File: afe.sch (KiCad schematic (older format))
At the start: 48 parts, among them J2 Conn_01x05, Q5 2N7002, Q6 2N7002, U10 TS5A2053, U11 ADS7946SRTET, U5 REF2915, U6 TCA9535MRGER, U7 TLV9062S, U8 OPA2322S, U9 TS5A2053

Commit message: *white smoke*
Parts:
- added C?: 100n, Capacitor_SMD:C_0603_1608Metric, symbol Device:C_Small
- added FB?: Ferret, symbol Device:Ferrite_Bead_Small
- added Q?: 2N7002, Package_TO_SOT_SMD:SOT-23, symbol Transistor_FET:2N7002
- added R?: 47k, Resistor_SMD:R_0603_1608Metric, symbol Device:R
- added U?: USBLC6-2SC6, Package_TO_SOT_SMD:SOT-23-6, symbol Power_Protection:USBLC6-2SC6
- R10, R9: value 100k -> 47k
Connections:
- net +3V3: now also U11.16 (DVDD), FB?.2, R?.2, U?.5 (VBUS)
- net AFE_ENABLE: now also Q?.1 (G)
- net GND: now also U11.17 (EPAD), Q?.2 (S), U?.2 (GND)
- net GNDA: now also C?.2; no longer C24.2, C25.2
- net PROBE1: now also U?.4 (IO2)
- net PROBE2: now also U?.3 (IO2)
- net ADC_CH_SEL: now reaches U11.11 (CH_SEL)
- net ADC_ENABLE: now reaches U11.12 (PDEN)
- net ADC_ENABLE: now also Q?.3 (D), R?.1
- net ADC_CS: now reaches U11.13 (~CS~)
- net ADC_SCK: now reaches U11.14 (SCLK)
- net ADC_MISO: now reaches U11.15 (SDO)
- net at U11.2 (AVDD): now also C?.1, FB?.1
- net at J2.3 (Pin_3), R11.1, R12.1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: no longer U7.7 (+)
- net at R12.2, U7.1, U7.2 (-): now also U7.7 (+)
- net ESP32_DAC: now reaches R10.2, R9.1, U7.3 (+)
- net at J2.1 (Pin_1), R18.1, R19.1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: now also U?.6 (IO1)
- net at J2.2 (Pin_2), R14.1, R15.1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: now also U?.1 (IO1)
- net PARTY_ENABLE: now reaches U6.7 (P06)
- net at Q5.3 (D), R28.1: now also C24.2
- net at Q6.3 (D), R29.1: now also C25.2
- net SCL renamed I2C_SCL
- net SDA renamed I2C_SDA
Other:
- note added: "Scope Mode:\n- enable reference buffer\n- use I2C to switch between ranges\n(0V to 5V, -6V to 6V, -65V to 65V)\n\nComponent Test Mode:\n- disable reference buffer\n- disable MUX\n- use I2C to create test sequence"
- note removed: "Scope Mode:\n- enable reference buffer\n- use I2C to switch between ranges\n(0V to 5V, -6V to 6V, -65V to 65V <- limited to +/- 60V by SSR)\n\nComponent Test Mode:\n- disable reference buffer\n- disable MUX\n- use I2C to create test sequence"
- moved on the sheet: H1, H2, H3, H4

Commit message: ADD: speaker
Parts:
- added C6: 4u7, symbol Device:CP_Small
- added LS1: Speaker, symbol Device:Speaker
- gave numbers to parts that had none: 5
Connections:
- net GND: now also LS1.2
- net at R12.2, U7.1, U7.2 (-)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: now also C6.1
- new net: C6.2, LS1.1
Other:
- note added: "Scope Mode:\n- set DAC pin to input\n- enable reference buffer\n- use I2C to switch between ranges\n(0V to 5V, -6V to 6V, -65V to 65V)\n\nComponent Test Mode:\n- disable reference buffer\n- disable MUX\n- use I2C to create test sequence"
- note removed: "Scope Mode:\n- enable reference buffer\n- use I2C to switch between ranges\n(0V to 5V, -6V to 6V, -65V to 65V)\n\nComponent Test Mode:\n- disable reference buffer\n- disable MUX\n- use I2C to create test sequence"
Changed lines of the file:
@@
 Connection ~ 1750 5450
 Text Notes 6700 4950 0    79   ~ 0
-Scope Mode:\n- enable reference buffer\n- use I2C to switch between ranges\n(0V to 5V, -6V to 6V, -65V to 65V)\n\nComponent Test Mode:\n- disable reference buffer\n- disable MUX\n- use I2C to create test sequence
+Scope Mode:\n- set DAC pin to input\n- enable reference buffer\n- use I2C to switch between ranges\n(0V to 5V, -6V to 6V, -65V to 65V)\n\nComponent Test Mode:\n- disable reference buffer\n- disable MUX\n- use I2C to create test sequence
 $Comp
 L power:GNDA #PWR043
@@
 ADC_SCK
 $Comp
-L power:GND #PWR?
+L power:GND #PWR068
 U 1 1 5C916289
 P 8800 2550
-F 0 "#PWR?" H 8800 2300 50  0001 C CNN
+F 0 "#PWR068" H 8800 2300 50  0001 C CNN
 F 1 "GND" V 8805 2377 50  0000 C CNN
 F 2 "" H 8800 2550 50  0001 C CNN
@@
 ADC_CS
 $Comp
-L power:+3.3V #PWR?
+L power:+3.3V #PWR067
 U 1 1 5C926BBE
 P 8800 950
-F 0 "#PWR?" H 8800 800 50  0001 C CNN
+F 0 "#PWR067" H 8800 800 50  0001 C CNN
 F 1 "+3.3V" H 8815 1123 50  0000 C CNN
 F 2 "" H 8800 950 50  0001 C CNN
@@
 $EndComp
 $Comp
-L Device:Ferrite_Bead_Small FB?
+L Device:Ferrite_Bead_Small FB1
 U 1 1 5C926F74
 P 8550 1050
-F 0 "FB?" V 8313 1050 50  0000 C CNN
+F 0 "FB1" V 8313 1050 50  0000 C CNN
 F 1 "Ferret" V 8404 1050 50  0000 C CNN
 F 2 "" V 8480 1050 50  0001 C CNN
@@
 	8650 1050 8750 1050
 $Comp
-L power:+3.3V #PWR?
+L power:+3.3V #PWR066
 U 1 1 5C92EEAE
 P 8300 950
-F 0 "#PWR?" H 8300 800 50  0001 C CNN
+F 0 "#PWR066" H 8300 800 50  0001 C CNN
 F 1 "+3.3V" H 8315 1123 50  0000 C CNN
 F 2 "" H 8300 950 50  0001 C CNN
@@
 $EndComp
 $Comp
-L power:GNDA #PWR?
+L power:GNDA #PWR065
 U 1 1 5C940215
 P 8100 1150
-F 0 "#PWR?" H 8100 900 50  0001 C CNN
+F 0 "#PWR065" H 8100 900 50  0001 C CNN
 F 1 "GNDA" V 8000 1000 50  0000 C CNN
 F 2 "" H 8100 1150 50  0001 C CNN
@@
 $EndComp
 $Comp
-L Device:C_Small C?
+L Device:C_Small C7
 U 1 1 5C94021B
 P 8200 1150
-F 0 "C?" V 8300 1100 50  0000 L CNN
+F 0 "C7" V 8300 1100 50  0000 L CNN
 F 1 "100n" V 8300 900 50  0000 L CNN
 F 2 "Capacitor_SMD:C_0603_1608Metric" H 8200 1150 50  0001 C CNN
@@
 ADC_CH_SEL
 $Comp
-L Power_Protection:USBLC6-2SC6 U?
+L Power_Protection:USBLC6-2SC6 U13
 U 1 1 5C9740D0
 P 5400 4900
-F 0 "U?" H 5500 5400 50  0000 C CNN
+F 0 "U13" H 5500 5400 50  0000 C CNN
 F 1 "USBLC6-2SC6" H 5750 5300 50  0000 C CNN
 F 2 "Package_TO_SOT_SMD:SOT-23-6" H 4650 5300 50  0001 C CNN
@@
 	4900 5000 4500 5000
 $Comp
-L power:GND #PWR?
+L power:GND #PWR062
 U 1 1 5C9857C3
 P 5400 5400
-F 0 "#PWR?" H 5400 5150 50  0001 C CNN
+F 0 "#PWR062" H 5400 5150 50  0001 C CNN
 F 1 "GND" H 5405 5227 50  0000 C CNN
 F 2 "" H 5400 5400 50  0001 C CNN
@@
 $EndComp
 $Comp
-L power:+3.3V #PWR?
+L power:+3.3V #PWR061
 U 1 1 5C985C77
 P 5400 4400
-F 0 "#PWR?" H 5400 4250 50  0001 C CNN
+F 0 "#PWR061" H 5400 4250 50  0001 C CNN
 F 1 "+3.3V" H 5415 4573 50  0000 C CNN
 F 2 "" H 5400 4400 50  0001 C CNN
@@
 PARTY_ENABLE
 $Comp
-L Transistor_FET:2N7002 Q?
+L Transistor_FET:2N7002 Q8
 U 1 1 5CAB9B10
 P 5900 3700
-F 0 "Q?" H 5650 3600 50  0000 L CNN
+F 0 "Q8" H 5650 3600 50  0000 L CNN
 F 1 "2N7002" H 5650 3500 50  0000 L CNN
 F 2 "Package_TO_SOT_SMD:SOT-23" H 6100 3625 50  0001 L CIN
@@
 	5850 3500 6000 3500
 $Comp
-L Device:R R?
+L Device:R R46
 U 1 1 5CACC0EF
 P 6000 3350
-F 0 "R?" H 5930 3304 50  0000 R CNN
+F 0 "R46" H 5930 3304 50  0000 R CNN
 F 1 "47k" H 5930 3395 50  0000 R CNN
 F 2 "Resistor_SMD:R_0603_1608Metric" V 5930 3350 50  0001 C CNN
@@
 Connection ~ 6000 3500
 $Comp
-L power:+3.3V #PWR?
+L power:+3.3V #PWR063
 U 1 1 5CACC921
 P 6000 3200
-F 0 "#PWR?" H 6000 3050 50  0001 C CNN
+F 0 "#PWR063" H 6000 3050 50  0001 C CNN
 F 1 "+3.3V" H 6015 3373 50  0000 C CNN
 F 2 "" H 6000 3200 50  0001 C CNN
@@
 $EndComp
 $Comp
-L power:GND #PWR?
+L power:GND #PWR064
 U 1 1 5CAD5AA6
 P 6000 3900
-F 0 "#PWR?" H 6000 3650 50  0001 C CNN
+F 0 "#PWR064" H 6000 3650 50  0001 C CNN
 F 1 "GND" H 6005 3727 50  0000 C CNN
 F 2 "" H 6000 3900 50  0001 C CNN
@@
 	1    0    0    -1
 $EndComp
+$Comp
+L Device:CP_Small C6
+U 1 1 5CB4B877
+P 1800 7100
+F 0 "C6" H 1888 7146 50  0000 L CNN
+F 1 "4u7" H 1888 7055 50  0000 L CNN
+F 2 "" H 1800 7100 50  0001 C CNN
+F 3 "~" H 1800 7100 50  0001 C CNN
+	1    1800 7100
+	1    0    0    -1
+$EndComp
+Wire Wire Line
+	1800 7000 1800 6900
+Connection ~ 1800 6900
+$Comp
+L Device:Speaker LS1
+U 1 1 5CB54E3A
+P 2250 7250
+F 0 "LS1" H 2420 7246 50  0000 L CNN
+F 1 "Speaker" H 2420 7155 50  0000 L CNN
+F 2 "" H 2250 7050 50  0001 C CNN
+F 3 "~" H 2240 7200 50  0001 C CNN
+	1    2250 7250
+	1    0    0    -1
+$EndComp
+$Comp
+L power:GND #PWR060
+U 1 1 5CB54F62
+P 1800 7350
+F 0 "#PWR060" H 1800 7100 50  0001 C CNN
+F 1 "GND" H 1805 7177 50  0000 C CNN
+F 2 "" H 1800 7350 50  0001 C CNN
+F 3 "" H 1800 7350 50  0001 C CNN
+	1    1800 7350
+	1    0    0    -1
+$EndComp
+Wire Wire Line
+	1800 7200 1800 7250
+Wire Wire Line
+	2050 7250 1800 7250
+Wire Wire Line
+	1800 7350 2050 7350
 $EndSCHEMATC

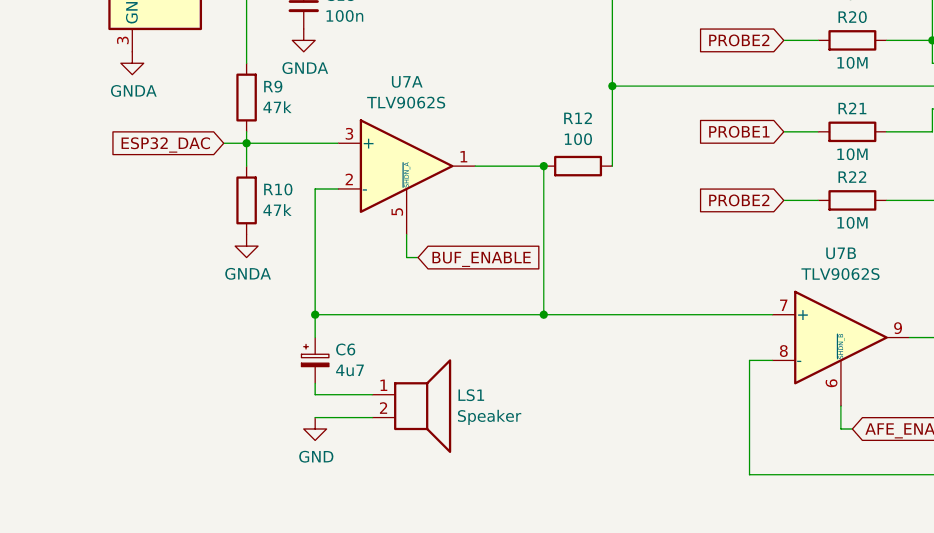
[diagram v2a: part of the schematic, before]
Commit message: ADD: speaker fet to make it compagtible to component tester mode
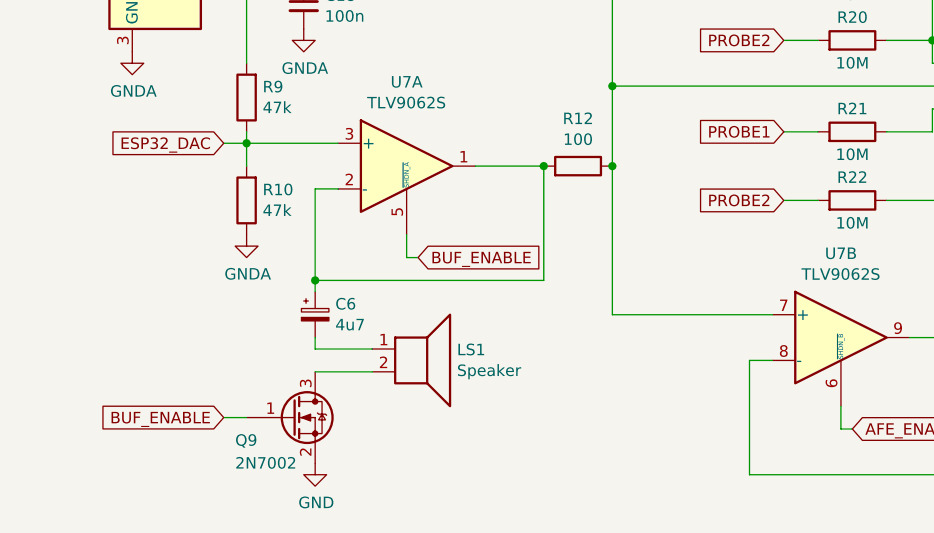
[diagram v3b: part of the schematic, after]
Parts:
- added Q9: 2N7002, Package_TO_SOT_SMD:SOT-23, symbol Transistor_FET:2N7002
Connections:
- net BUF_ENABLE: now also Q9.1 (G)
- net GND: now also Q9.2 (S); no longer LS1.2
- net at J2.3 (Pin_3), R11.1, R12.1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: now also U7.7 (+)
- net at C6.1, R12.2, U7.1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: no longer U7.7 (+)
- new net: LS1.2, Q9.3 (D)
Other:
- moved on the sheet: C6, LS1
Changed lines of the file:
@@
 	1900 6350 1800 6350
-Wire Wire Line
-	1800 6350 1800 6900
-Wire Wire Line
-	1800 6900 2800 6900
-Wire Wire Line
-	2800 6900 2800 6250
 Wire Wire Line
 	1500 5450 1500 5800
@@
 	7400 2700 7300 2700
 Connection ~ 7300 900
-Connection ~ 2800 6250
 Wire Wire Line
 	1500 5450 1400 5450
@@
 	6650 2600 7100 2600
 Connection ~ 7100 2600
-Wire Wire Line
-	2800 6900 3800 6900
-Connection ~ 2800 6900
 Text GLabel 1400 6150 0    50   Input ~ 0
 ESP32_DAC
@@
 L Device:CP_Small C6
 U 1 1 5CB4B877
-P 1800 7100
-F 0 "C6" H 1888 7146 50  0000 L CNN
-F 1 "4u7" H 1888 7055 50  0000 L CNN
-F 2 "" H 1800 7100 50  0001 C CNN
-F 3 "~" H 1800 7100 50  0001 C CNN
-	1    1800 7100
-	1    0    0    -1
-$EndComp
-Wire Wire Line
-	1800 7000 1800 6900
-Connection ~ 1800 6900
+P 1800 6900
+F 0 "C6" H 1888 6946 50  0000 L CNN
+F 1 "4u7" H 1888 6855 50  0000 L CNN
+F 2 "" H 1800 6900 50  0001 C CNN
+F 3 "~" H 1800 6900 50  0001 C CNN
+	1    1800 6900
+	1    0    0    -1
+$EndComp
 $Comp
 L Device:Speaker LS1
 U 1 1 5CB54E3A
-P 2250 7250
-F 0 "LS1" H 2420 7246 50  0000 L CNN
-F 1 "Speaker" H 2420 7155 50  0000 L CNN
-F 2 "" H 2250 7050 50  0001 C CNN
-F 3 "~" H 2240 7200 50  0001 C CNN
-	1    2250 7250
-	1    0    0    -1
-$EndComp
+P 2250 7050
+F 0 "LS1" H 2420 7046 50  0000 L CNN
+F 1 "Speaker" H 2420 6955 50  0000 L CNN
+F 2 "" H 2250 6850 50  0001 C CNN
+F 3 "~" H 2240 7000 50  0001 C CNN
+	1    2250 7050
+	1    0    0    -1
+$EndComp
+Wire Wire Line
+	1800 7000 1800 7050
+Wire Wire Line
+	2050 7050 1800 7050
+Wire Wire Line
+	1800 7150 2050 7150
+Wire Wire Line
+	3100 6250 3100 6900
+Wire Wire Line
+	3100 6900 3800 6900
+Connection ~ 3100 6250
+Wire Wire Line
+	2800 6250 2800 6750
+Wire Wire Line
+	2800 6750 1800 6750
+Wire Wire Line
+	1800 6750 1800 6350
+Connection ~ 2800 6250
+Wire Wire Line
+	1800 6800 1800 6750
+Connection ~ 1800 6750
+$Comp
+L Transistor_FET:2N7002 Q9
+U 1 1 5CBA6288
+P 1700 7350
+F 0 "Q9" H 1450 7250 50  0000 L CNN
+F 1 "2N7002" H 1450 7150 50  0000 L CNN
+F 2 "Package_TO_SOT_SMD:SOT-23" H 1900 7275 50  0001 L CIN
+F 3 "https://www.fairchildsemi.com/datasheets/2N/2N7002.pdf" H 1700 7350 50  0001 L CNN
+	1    1700 7350
+	1    0    0    -1
+$EndComp
+Wire Wire Line
+	1400 7350 1500 7350
 $Comp
 L power:GND #PWR060
-U 1 1 5CB54F62
-P 1800 7350
-F 0 "#PWR060" H 1800 7100 50  0001 C CNN
-F 1 "GND" H 1805 7177 50  0000 C CNN
-F 2 "" H 1800 7350 50  0001 C CNN
-F 3 "" H 1800 7350 50  0001 C CNN
-	1    1800 7350
-	1    0    0    -1
-$EndComp
-Wire Wire Line
-	1800 7200 1800 7250
-Wire Wire Line
-	2050 7250 1800 7250
-Wire Wire Line
-	1800 7350 2050 7350
+U 1 1 5CBA6291
+P 1800 7550
+F 0 "#PWR060" H 1800 7300 50  0001 C CNN
+F 1 "GND" H 1805 7377 50  0000 C CNN
+F 2 "" H 1800 7550 50  0001 C CNN
+F 3 "" H 1800 7550 50  0001 C CNN
+	1    1800 7550
+	1    0    0    -1
+$EndComp
+Text GLabel 1400 7350 0    50   Input ~ 0
+BUF_ENABLE
 $EndSCHEMATC
